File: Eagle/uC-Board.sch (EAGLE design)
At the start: 12 parts, among them IC1 7805T, J1 YAESU CAT, J2 ICOM CIV, J3 SWITCHES, J4 DISPLAY, J5 ROTARY, J6 PTT IN, J7 PTT OUT, X1 PWR IN

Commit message: Display and LEDs
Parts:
- removed X1: PWR IN, con-molex:22-23-2031
- added J8: PWR IN, con-molex:22-23-2031
- added Q1: BC557, transistor-pnp:BC557
- added R1, R2, R3: (no value), rcl:R-EU_0207/10
- J1: value YAESU CAT -> SWITCHES; device con-molex:22-27-2031-03 -> con-molex:22-27-2041-04
- J2: value ICOM CIV -> ROTARY; device con-molex:22-27-2021-02 -> con-molex:22-27-2051-05
- J3: value SWITCHES -> DISPLAY; device con-molex:22-27-2051-05 -> con-molex:22-27-2081-08
- J4: value DISPLAY -> ICOM CIV; device con-molex:22-27-2101-10 -> con-molex:22-27-2021-02
- J5: value ROTARY -> PTT IN; device con-molex:22-27-2051-05 -> con-molex:22-27-2021-02
- J6: value PTT IN -> YAESU CAT; device con-molex:22-27-2021-02 -> con-molex:22-27-2031-03
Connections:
- new net N$1: J3-6.S, U$1.18/A4/T/SDA0
- new net N$10: Q1.B, R1.2, R2.1
- new net N$11: Q1.E, R3.2
- new net N$12: J5-1.S, R1.1
- new net N$2: J3-5.S, U$1.19/A5/T/SCL0
- new net N$3: J3-4.S, U$1.20/A6/PWM
- new net N$7: J3-3.S, U$1.21/A7/PWM
- new net N$8: J3-2.S, U$1.22/A8/T/PWM
- new net N$9: J3-1.S, U$1.23/A9/T/PWM
- net +12V: now also J8-1.S; no longer X1-1.S
- net +5V: now also Q1.C, R2.2
- net GND: now also J3-8.S, J4-2.S, J5-2.S, J6-2.S, J8-3.S, R3.1; no longer J1-2.S, J2-2.S, X1-3.S
- net N$4: now also J4-1.S; no longer J2-1.S
- net N$5: now also J6-1.S; no longer J1-1.S
- net N$6: now also J6-3.S; no longer J1-3.S
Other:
- moved on the sheet: C1, C2, IC1, J1-1, J1-2, J1-3, J2-1, J2-2, J3-1, J3-2, J3-3, J3-4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

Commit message: added more components, corrections
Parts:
- added IC2, IC3: UDN2981A, uln-udn:UDN2981A
- added IC4: ULN2803A, uln-udn:ULN2803A
- added J10: REL2, con-molex:22-27-2021-02
- added J11: REL3, con-molex:22-27-2021-02
- added J9: REL1, con-molex:22-27-2021-02
- added Q2: BS170, transistor-small-signal:BS170
- added R4, R5, R6, R7, R8: (no value), rcl:R-EU_0207/10
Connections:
- new net N$13: J1-1.S, U$1.4/CAN-RX-PWM
- new net N$14: Q2.G, R4.2
- new net N$15: J7-1.S, Q2.D
- new net N$16: J2-1.S, U$1.17/A3/T
- new net N$17: J2-2.S, U$1.16/A2/T
- new net N$18: J2-3.S, U$1.15/A1/T
- new net N$19: J1-2.S, U$1.3/CAN-TX/PWM
- new net N$20: J1-3.S, U$1.2
- new net N$21: IC2.I5, U$1.23/A9/T/PWM
- new net N$22: IC2.I6, U$1.22/A8/T/PWM
- new net N$23: IC2.I7, U$1.21/A7/PWM
- new net N$24: IC2.I8, U$1.20/A6/PWM
- new net N$25: J3-4.S, R8.2
- new net N$26: J3-3.S, R7.2
- new net N$27: J3-2.S, R6.2
- new net N$28: J3-1.S, R5.2
- net +5V: now also IC2.VS, J3-7.S
- net GND: now also IC2.GND, IC3.GND, IC4.GND, J2-5.S, J7-2.S, Q2.S
- net N$11: now also R4.1
- net N$3: now also IC2.O8, R8.1; no longer J3-4.S, U$1.20/A6/PWM
- net N$7: now also IC2.O7, R7.1; no longer J3-3.S, U$1.21/A7/PWM
- net N$8: now also IC2.O6, R6.1; no longer J3-2.S, U$1.22/A8/T/PWM
- net N$9: now also IC2.O5, R5.1; no longer J3-1.S, U$1.23/A9/T/PWM
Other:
- moved on the sheet: J1-1, J1-2, J1-3, J1-4, J2-1, J2-2, J2-3, J2-4, J2-5, J3-1, J3-2, J3-3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

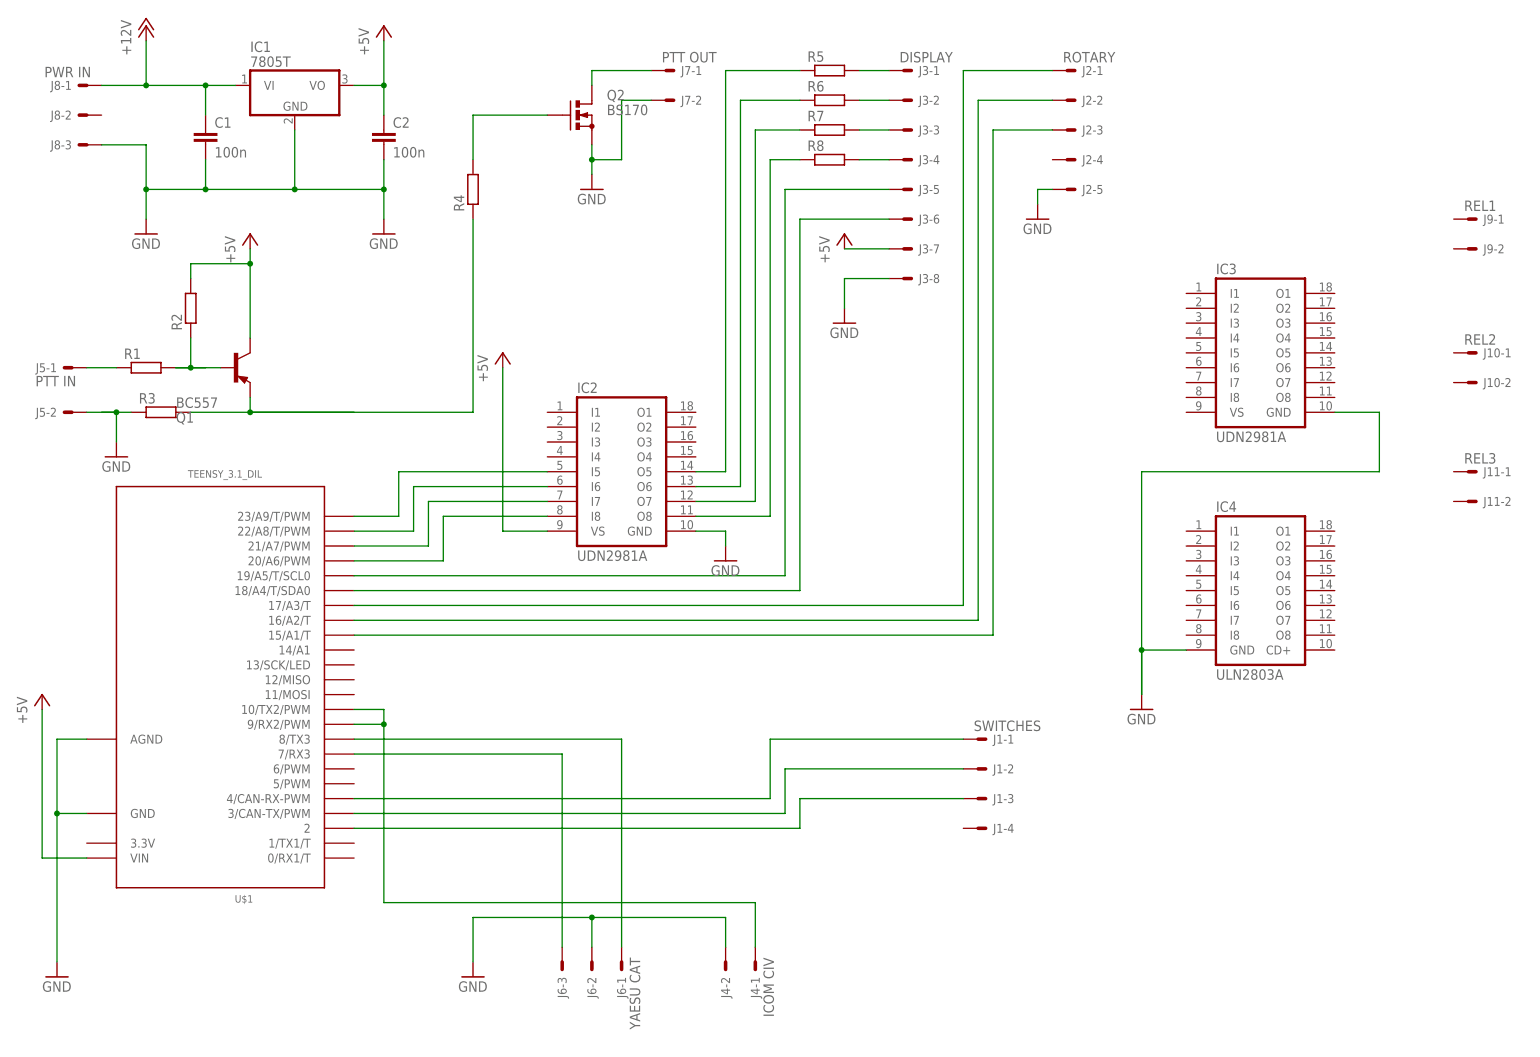
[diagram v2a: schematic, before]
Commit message: added LED and missing capacitors; completed resistor values
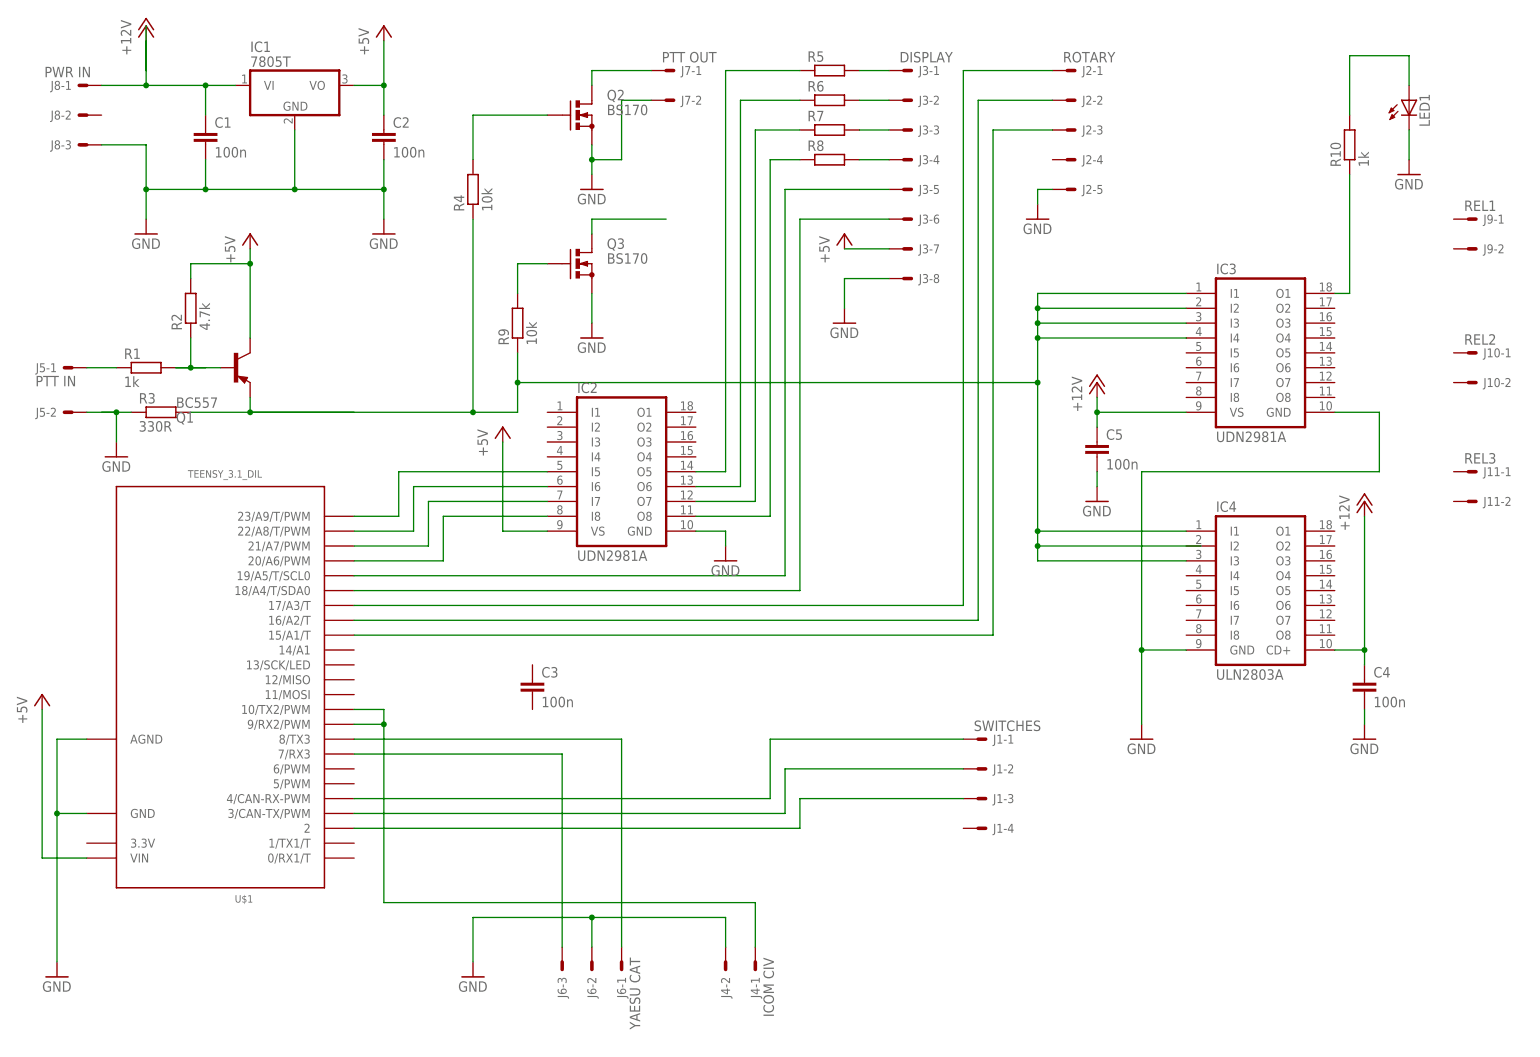
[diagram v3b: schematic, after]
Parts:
- added C3, C4, C5: 100n, rcl:C-EU025-025X050
- added LED1: (no value), led:LED5MM
- added Q3: BS170, transistor-small-signal:BS170
- added R10: 1k, rcl:R-EU_0207/10
- added R9: 10k, rcl:R-EU_0207/10
- R1: value (none) -> 1k
- R2: value (none) -> 4.7k
- R3: value (none) -> 330R
- R4: value (none) -> 10k
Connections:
- removed net N$11: Q1.E, R3.2, R4.1
- new net N$29: Q3.G, R9.2
- new net N$30: Q3.D
- new net N$31: LED1.A, R10.2
- new net N$32: IC3.O1, R10.1
- new net N$34: IC3.I1, IC3.I2, IC3.I3, IC3.I4, IC4.I1, IC4.I3, Q1.E, R3.2, R4.1, R9.1
- net +12V: now also C4.1, C5.1, IC3.VS, IC4.CD+
- net GND: now also C4.2, C5.2, LED1.C, Q3.S
